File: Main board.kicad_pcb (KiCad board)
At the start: 4 copper layers, 50 x 75 mm, 106 parts, among them CN1 PA001-6P, CN2 PA001-6P, J1 Conn_ARM_SWD_TagConnect_TC203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, J2 Conn_01x02_Pin, J3 Conn_01x02_Pin, J5 Connector, USB-TYPE-C-16P, J6 436500201, J7 Conn_01x02_Pin, J8 Conn_01x04_Pin, Q1 SI7232DN-T1-GE3, Q2 SI7232DN-T1-GE3, SW1 SKRKAEE020, SW2 SKRKAEE020, SW3 SW_SPDT, SW4 SW_SPDT, U1 STM32U575VGTx, U10 TLV75733PDBV, U11 NRVB120VLSFT1G, U12 NRVB120VLSFT1G, U2 TPS62901RPJR, U3 MS5607-02BA03, U7 SN74AHCT125DR, U9 ICM-45686, X1 1XXD32000MBA, Y1 ECS-327TXO-33-TR

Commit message: Changed Pyro pour
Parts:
- moved J2 9.08 mm to (140.4, 102.1)
- moved SW3 2.01 mm to (133.4, 115.2)
- moved R5 1.40 mm to (139.7, 116.9)
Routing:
- net BEC+: track 14.2 -> 1.08 mm
- net PYRO+: track 5.84 -> 0.00 mm
- net Net-(SW3-B): track 4.69 -> 6.17 mm
- added copper zone on In2.Cu, net PYRO+
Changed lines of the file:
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@@
 	(footprint "PCM_JLCPCB:R_0402"
 		(layer "F.Cu")
-		(at 138.3067 116.7731)
+		(at 139.7 116.9)
 		(descr "Resistor SMD 0402 (1005 Metric), square (rectangular) end terminal, IPC_7351 nominal, (Body size source: IPC-SM-782 page 72, https://www.pcb-3d.com/wordpress/wp-content/uploads/ipc-sm-782a_amendment_1_and_2.pdf), generated with kicad-footprint-generator")
 		(tags "resistor")
@@
 	(footprint "Connector_PinHeader_2.54mm:PinHeader_1x02_P2.54mm_Vertical"
 		(layer "F.Cu")
-		(at 139.675 111.15 -90)
+		(at 140.375 102.1 -90)
 		(descr "Through hole straight pin header, 1x02, 2.54mm pitch, single row")
 		(tags "Through hole pin header THT 1x02 2.54mm single row")
@@
 	(footprint "EasyEDA:SW-TH_3P-L8.8-W3.9-P2.50_SS12D00G3"
 		(layer "F.Cu")
-		(at 131.4 115.4 180)
+		(at 133.4 115.2 180)
 		(property "Reference" "SW3"
 			(at 0 -4 0)
@@
 	)
 	(segment
-		(start 157.1675 120.8625)
-		(end 157.1675 123.3825)
-		(width 2)
-		(layer "F.Cu")
-		(net 10)
-	)
-	(segment
-		(start 124.251501 82.3736)
-		(end 123.827501 82.7976)
+		(start 133.4 115.2)
+		(end 133.4 117.3)
 		(width 2.5)
 		(layer "F.Cu")
-		(net 10)
+		(net 20)
 	)
 	(segment
-		(start 126.945001 82.3736)
-		(end 124.251501 82.3736)
+		(start 133.4 117.3)
+		(end 132.1675 118.5325)
 		(width 2.5)
 		(layer "F.Cu")
-		(net 10)
-	)
-	(segment
-		(start 157.1675 123.3825)
-		(end 157.15 123.4)
-		(width 2)
-		(layer "F.Cu")
-		(net 10)
+		(net 20)
 	)
 	(segment
-		(start 131.4 115.4)
-		(end 131.4 120.095)
-		(width 2)
+		(start 132.1675 118.5325)
+		(end 132.1675 120.8625)
+		(width 2.5)
 		(layer "F.Cu")
 		(net 20)
@@
 	)
 	(segment
-		(start 137.135 111.15)
-		(end 137.135 108.879869)
-		(width 2)
-		(layer "In2.Cu")
-		(net 36)
-	)
-	(segment
-		(start 137.135 111.15)
-		(end 137.135 112.165)
-		(width 2)
-		(layer "In2.Cu")
-		(net 36)
-	)
-	(segment
-		(start 137.135 112.165)
-		(end 133.9 115.4)
-		(width 2)
-		(layer "In2.Cu")
-		(net 36)
-	)
-	(segment
 		(start 133.405131 105.15)
 		(end 132.327501 105.15)
@@
 	)
 	(segment
-		(start 137.135 108.879869)
-		(end 133.405131 105.15)
-		(width 2)
-		(layer "In2.Cu")
-		(net 36)
-	)
-	(segment
 		(start 144.314401 92.096)
 		(end 144.244337 92.166064)
@@
 	)
 	(zone
-		(net 10)
-		(net_name "PYRO+")
+		(net 65)
+		(net_name "MS5607_CS")
 		(layer "F.Cu")
-		(name "PYRO+")
-		(hatch full 0.5)
+		(name "$teardrop_padvia$")
+		(hatch none 0.1)
+		(priority 30002)
+		(attr
+			(teardrop
+				(type padvia)
+			)
+		)
 		(connect_pads yes
 			(clearance 0)
 		)
-		(min_thickness 0.25)
+		(min_thickness 0.0254)
 		(filled_areas_thickness no)
 		(fill yes
 			(thermal_gap 0.5)
 			(thermal_bridge_width 0.5)
+			(island_removal_mode 1)
+			(island_area_min 10)
 		)
 		(polygon
 			(pts
-				(xy 160.65 123.15) (xy 161.65 123.65) (xy 161.65 126.4) (xy 121.9 126.4) (xy 121.4 125.9) (xy 121.4 123.15)
-				(xy 121.65 116.65) (xy 129.4 117.4) (xy 129.65 123.4)
+				(xy 144.04 72.509546) (xy 144.24 72.509546) (xy 144.49 72.159546) (xy 144.14 71.558546) (xy 143.79 72.159546)
 			)
 		)
@@
 	)
 	(zone
-		(net 65)
-		(net_name "MS5607_CS")
+		(net 135)
+		(net_name "HSE_IN")
 		(layer "F.Cu")
 		(name "$teardrop_padvia$")
 		(hatch none 0.1)
-		(priority 30001)
+		(priority 30006)
 		(attr
 			(teardrop
@@
 		(polygon
 			(pts
-				(xy 144.04 72.509546) (xy 144.24 72.509546) (xy 144.49 72.159546) (xy 144.14 71.558546) (xy 143.79 72.159546)
+				(xy 142.775382 85.696) (xy 142.775382 85.496) (xy 142.425382 85.469117) (xy 142.074382 85.919117)
+				(xy 142.425382 86.142719)
 			)
 		)
@@
 	)
 	(zone
-		(net 65)
-		(net_name "MS5607_CS")
+		(net 104)
+		(net_name "LSE_IN")
 		(layer "F.Cu")
 		(name "$teardrop_padvia$")
@@
 		(polygon
 			(pts
-				(xy 144.24 72.809546) (xy 144.04 72.809546) (xy 143.79 73.159546) (xy 144.14 73.760546) (xy 144.49 73.159546)
+				(xy 141.534391 83.696001) (xy 141.534391 83.496001) (xy 141.034391 82.991268) (xy 140.508391 83.3997)
+				(xy 141.034391 83.8997)
 			)
 		)
 	)
 	(zone
-		(net 10)
-		(net_name "PYRO+")
+		(net 1)
+		(net_name "VBAT-")
 		(layer "F.Cu")
-		(name "PYRO+")
-		(hatch full 0.5)
+		(name "$teardrop_padvia$")
+		(hatch none 0.1)
+		(priority 30004)
+		(attr
+			(teardrop
+				(type padvia)
+			)
+		)
 		(connect_pads yes
 			(clearance 0)
 		)
-		(min_thickness 0.25)
+		(min_thickness 0.0254)
 		(filled_areas_thickness no)
 		(fill yes
 			(thermal_gap 0.5)
 			(thermal_bridge_width 0.5)
+			(island_removal_mode 1)
+			(island_area_min 10)
 		)
 		(polygon
 			(pts
-				(xy 124.794282 108.224472) (xy 128.353932 110.735673) (xy 131.15 109.15) (xy 133.533755 109.15)
-				(xy 133.991865 109.774999) (xy 133.4 111.65) (xy 129.9 112.9) (xy 129.4 119.15) (xy 121.4 119.15)
-				(xy 121.527306 75.349634) (xy 122.600657 74.276283) (xy 126.480883 74.202008) (xy 127.414901 75.154949)
-				(xy 127.323018 77.497975) (xy 126.729101 78.095) (xy 124.456342 78.095)
+				(xy 145.95 71.459547) (xy 145.950001 71.659546) (xy 146.3 71.909546) (xy 146.650999 71.559546) (xy 146.3 71.209546)
 			)
 		)
@@
 	)
 	(zone
-		(net 135)
-		(net_name "HSE_IN")
-		(layer "F.Cu")
-		(name "$teardrop_padvia$")
-		(hatch none 0.1)
-		(priority 30001)
-		(attr
-			(teardrop
-				(type padvia)
-			)
-		)
-		(connect_pads yes
-			(clearance 0)
-		)
-		(min_thickness 0.0254)
-		(filled_areas_thickness no)
-		(fill yes
-			(thermal_gap 0.5)
-			(thermal_bridge_width 0.5)
-			(island_removal_mode 1)
-			(island_area_min 10)
-		)
-		(polygon
-			(pts
-				(xy 142.775382 85.696) (xy 142.775382 85.496) (xy 142.425382 85.469117) (xy 142.074382 85.919117)
-				(xy 142.425382 86.142719)
-			)
-		)
-	)
-	(zone
 		(net 10)
 		(net_name "PYRO+")
@@
 		(name "$teardrop_padvia$")
 		(hatch none 0.1)
-		(priority 30004)
+		(priority 30005)
 		(attr
 			(teardrop
@@
 	)
 	(zone
-		(net 104)
-		(net_name "LSE_IN")
-		(layer "F.Cu")
-		(name "$teardrop_padvia$")
-		(hatch none 0.1)
-		(priority 30000)
-		(attr
-			(teardrop
-				(type padvia)
-			)
-		)
-		(connect_pads yes
-			(clearance 0)
-		)
-		(min_thickness 0.0254)
-		(filled_areas_thickness no)
-		(fill yes
-			(thermal_gap 0.5)
-			(thermal_bridge_width 0.5)
-			(island_removal_mode 1)
-			(island_area_min 10)
-		)
-		(polygon
-			(pts
-				(xy 141.534391 83.696001) (xy 141.534391 83.496001) (xy 141.034391 82.991268) (xy 140.508391 83.3997)
-				(xy 141.034391 83.8997)
-			)
-		)
-	)
-	(zone
-		(net 28)
-		(net_name "Net-(D4-A)")
+		(net 141)
+		(net_name "Net-(CN2-Pad3)")
 		(layer "F.Cu")
-		(name "$teardrop_padvia$")
-		(hatch none 0.1)
-		(priority 30002)
-		(attr
-			(teardrop
-				(type padvia)
-			)
-		)
+		(name "CN2-Pad3")
+		(hatch full 0.5)
+		(priority 4)
 		(connect_pads yes
 			(clearance 0)
 		)
-		(min_thickness 0.0254)
+		(min_thickness 0.25)
 		(filled_areas_thickness no)
 		(fill yes
 			(thermal_gap 0.5)
 			(thermal_bridge_width 0.5)
-			(island_removal_mode 1)
-			(island_area_min 10)
 		)
 		(polygon
 			(pts
-				(xy 143.120002 69.159547) (xy 143.120002 69.359547) (xy 143.520002 69.659547) (xy 143.921002 69.259548)
-				(xy 143.520002 68.859548)
+				(xy 132.577501 84.5476) (xy 133.827501 84.5476) (xy 133.827501 88.7671) (xy 132.577501 88.7671)
 			)
 		)
 	)
 	(zone
-		(net 141)
-		(net_name "Net-(CN2-Pad3)")
+		(net 139)
+		(net_name "Net-(CN1-Pad5)")
 		(layer "F.Cu")
-		(name "CN2-Pad3")
+		(name "CN1-Pad3")
 		(hatch full 0.5)
 		(priority 4)
@@
 		(polygon
 			(pts
-				(xy 132.577501 84.5476) (xy 133.827501 84.5476) (xy 133.827501 88.7671) (xy 132.577501 88.7671)
+				(xy 156.3692 115.5793) (xy 156.3692 116.829301) (xy 152.1497 116.829301) (xy 152.1497 115.5793)
 			)
 		)
 	)
 	(zone
-		(net 139)
-		(net_name "Net-(CN1-Pad5)")
+		(net 28)
+		(net_name "Net-(D4-A)")
 		(layer "F.Cu")
-		(name "CN1-Pad3")
-		(hatch full 0.5)
-		(priority 4)
+		(name "$teardrop_padvia$")
+		(hatch none 0.1)
+		(priority 30003)
+		(attr
+			(teardrop
+				(type padvia)
+			)
+		)
 		(connect_pads yes
 			(clearance 0)
 		)
-		(min_thickness 0.25)
+		(min_thickness 0.0254)
 		(filled_areas_thickness no)
 		(fill yes
 			(thermal_gap 0.5)
 			(thermal_bridge_width 0.5)
+			(island_removal_mode 1)
+			(island_area_min 10)
 		)
 		(polygon
 			(pts
-				(xy 156.3692 115.5793) (xy 156.3692 116.829301) (xy 152.1497 116.829301) (xy 152.1497 115.5793)
+				(xy 143.120002 69.159547) (xy 143.120002 69.359547) (xy 143.520002 69.659547) (xy 143.921002 69.259548)
+				(xy 143.520002 68.859548)
 			)
 		)
@@
 	)
 	(zone
-		(net 1)
-		(net_name "VBAT-")
+		(net 65)
+		(net_name "MS5607_CS")
 		(layer "F.Cu")
 		(name "$teardrop_padvia$")
 		(hatch none 0.1)
-		(priority 30003)
+		(priority 30001)
 		(attr
 			(teardrop
@@
 		(polygon
 			(pts
-				(xy 145.95 71.459547) (xy 145.950001 71.659546) (xy 146.3 71.909546) (xy 146.650999 71.559546) (xy 146.3 71.209546)
+				(xy 144.24 72.809546) (xy 144.04 72.809546) (xy 143.79 73.159546) (xy 144.14 73.760546) (xy 144.49 73.159546)
+			)
+		)
+	)
+	(zone
+		(net 10)
+		(net_name "PYRO+")
+		(layer "In2.Cu")
+		(name "PYRO+")
+		(hatch full 0.5)
+		(priority 6)
+		(connect_pads yes
+			(clearance 0.6)
+		)
+		(min_thickness 0.25)
+		(filled_areas_thickness no)
+		(fill yes
+			(thermal_gap 0.5)
+			(thermal_bridge_width 0.5)
+		)
+		(polygon
+			(pts
+				(xy 121.65 73.65) (xy 129.8 73.65) (xy 130.7 74.55) (xy 130.410508 112.039213) (xy 132.783966 116.8493)
+				(xy 159.6 118.3) (xy 159.7 118.4) (xy 159.7 126.2) (xy 159.5 126.4) (xy 128.3 126.4) (xy 128.1 126.2)
+				(xy 128.1 120.8625) (xy 126.7375 119.5) (xy 122.4 119.5) (xy 121.3 118.4) (xy 121.3 73.9)
 			)
 		)

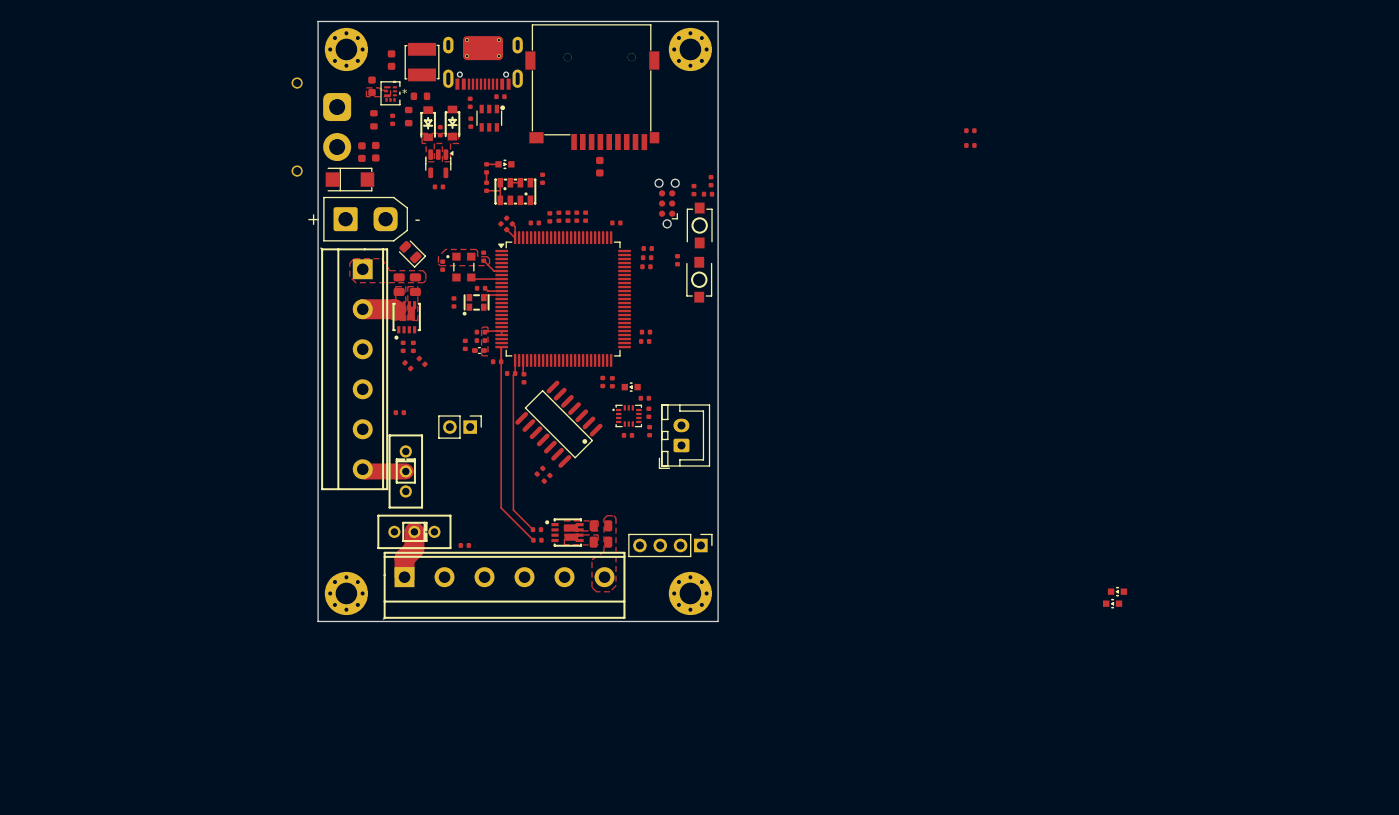
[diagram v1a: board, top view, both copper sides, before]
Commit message: Change switch footprint to C&K 1101M2S3CQE2
For handling PYRO power and temp
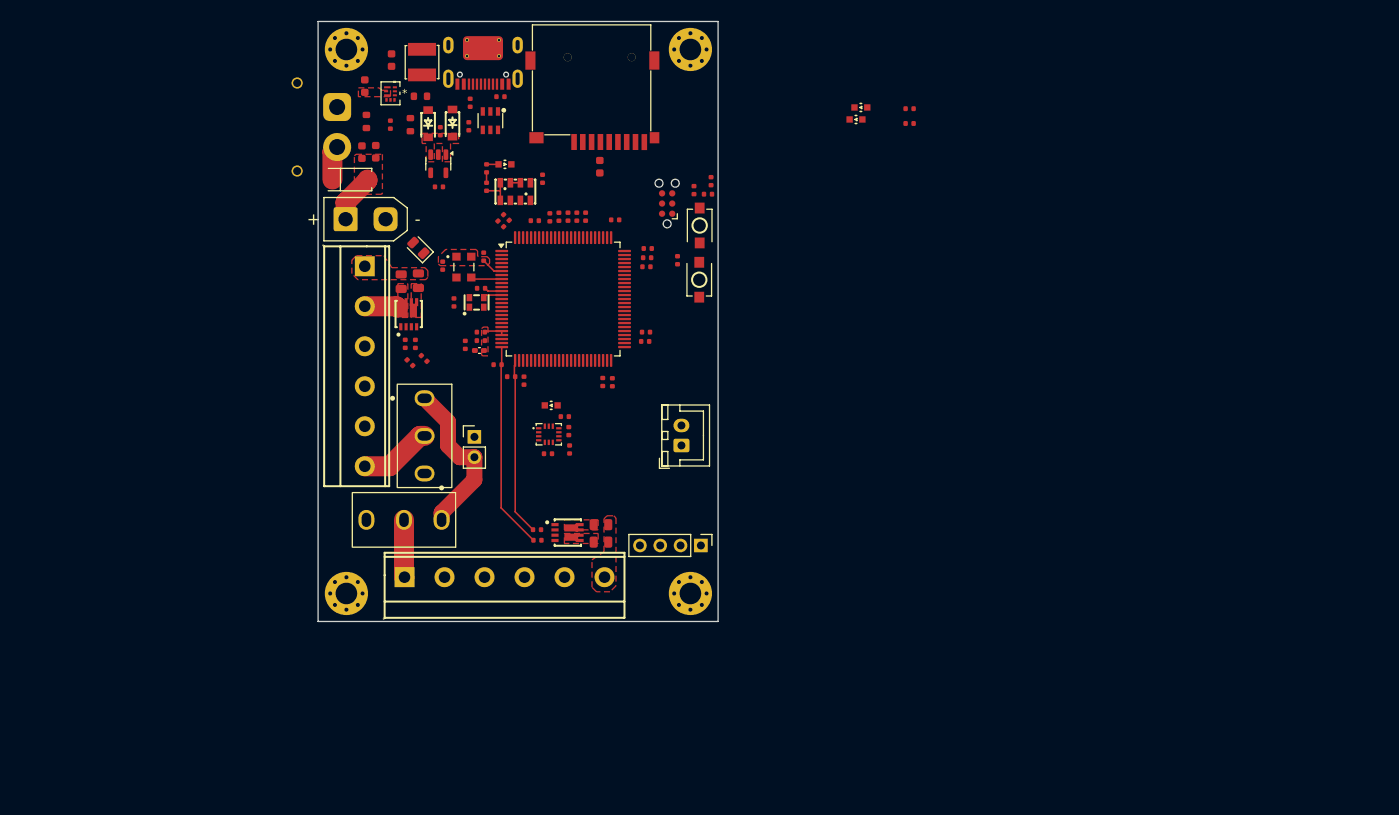
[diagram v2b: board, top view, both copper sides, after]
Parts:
- removed C15: 100nF, PCM_JLCPCB:C_0402
- removed C25: 10uF, PCM_JLCPCB:C_0402
- removed R5, R8: 75Ω, PCM_JLCPCB:R_0402
- removed U7: SN74AHCT125DR, EASYEDA:SOIC-14_L8.7-W3.9-P1.27-LS6.0-BL
- J6: value 436500201 -> XT30UPB-F
- SW3, SW4: footprint EasyEDA:SW-TH_3P-L8.8-W3.9-P2.50_SS12D00G3 -> Mainboard_local:SW-TH_1101M2S3CQE2
- moved D6 68.5 mm to (188.6, 63.6)
- moved D5 68.5 mm to (189.2, 62.1)
- moved C17 10.3 mm to (150.1, 105.4)
- moved C19 10.3 mm to (152.8, 104.9)
- moved D7 10.3 mm to (150.5, 99.4)
- moved R18 10.3 mm to (152.2, 100.8)
- moved U9 10.3 mm to (150.2, 103.0)
- moved R31 10.3 mm to (152.7, 102.6)
- moved R14 8.08 mm to (195.3, 64.2)
- moved R6 8.08 mm to (195.3, 62.3)
- moved SW4 5.03 mm to (134.7, 103.2)
- moved SW3 1.98 mm to (132.1, 113.7)
- moved J2 1.33 mm to (140.9, 103.3), turned to 0 degrees
- moved JP1 1.12 mm to (133.9, 79.7)
- moved R24 1.04 mm to (132.9, 64.3)
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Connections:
- U1 pad 40: PWM1 -> SERVO1
- U1 pad 42: PWM2 -> SERVO2
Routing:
- net BEC+: track 1.08 -> 20.6 mm
- net PYRO+: track 0.00 -> 6.09 mm
- net +3V3: track 11.4 -> 6.36 mm
- net VBAT+: track 0.00 -> 4.31 mm
- net Net-(SW4-B): track 5.50 -> 9.04 mm
- net FIRE_A: track 22.3 -> 20.0 mm
- net Net-(SW3-B): track 6.17 -> 7.19 mm

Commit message: New layout New.ioc
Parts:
- CN1, CN2: value PA001-6P -> KF127S-3.5-6P; footprint Mainboard_local:CONN-TH_6P-P5.00_PA001-6P -> TerminalBlock_Phoenix:TerminalBlock_Phoenix_PT-1,5-6-3.5-H_1x06_P3.50mm_Horizontal
- H1, H2, H3, H4: footprint MountingHole:MountingHole_2.7mm_M2.5_Pad_Via -> MountingHole:MountingHole_2.2mm_M2_Pad_Via
- J3: value Conn_01x02_Pin -> Micro-Fit 43650-0215; footprint Connector_AMASS:AMASS_XT30PW-F_1x02_P2.50mm_Horizontal -> Connector_Molex:Molex_Micro-Fit_3.0_43650-0215_1x02_P3.00mm_Vertical; moved to F.Cu
- J6: value XT30UPB-F -> Micro-Fit 43650-0215; footprint Connector_AMASS:AMASS_XT30UPB-F_1x02_P5.0mm_Vertical -> Connector_Molex:Molex_Micro-Fit_3.0_43650-0215_1x02_P3.00mm_Vertical
- JP3: renamed from SW3; value SW_SPDT -> BEC 1-2 / PYRO 2-3; footprint Mainboard_local:SW-TH_1101M2S3CQE2 -> Jumper:SolderJumper-3_P1.3mm_Open_Pad1.0x1.5mm_NumberLabels
- JP4: renamed from SW4; value SW_SPDT -> BEC 1-2 / PYRO 2-3; footprint Mainboard_local:SW-TH_1101M2S3CQE2 -> Jumper:SolderJumper-3_P1.3mm_Open_Pad1.0x1.5mm_NumberLabels
- moved C17 104.0 mm to (245.3, 63.6)
- moved R18 104.0 mm to (247.4, 59.0)
- moved U9 104.0 mm to (245.4, 61.2)
- moved R31 104.0 mm to (247.9, 60.8)
- moved C19 104.0 mm to (248.0, 63.1)
- moved D7 104.0 mm to (245.7, 57.5)
- moved C28 96.1 mm to (205.4, 116.5), turned to 0 degrees
- moved L1 95.3 mm to (205.2, 120.3), turned to 180 degrees
- moved J5 95.0 mm to (204.9, 127.9), turned to 90 degrees
- moved C27 92.2 mm to (202.2, 113.1), turned to 0 degrees
- moved U2 90.3 mm to (201.3, 116.3), turned to -90 degrees
- moved R22 89.5 mm to (200.8, 130.1), turned to -90 degrees
- moved R26 89.3 mm to (200.9, 120.1), turned to 90 degrees
- moved R23 88.1 mm to (200.1, 126.3), turned to 180 degrees
- moved R25 86.0 mm to (197.7, 113.3), turned to 180 degrees
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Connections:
- CN1 pad 1: Net-(SW3-B) -> Net-(CN1-Pad1)
- CN1 pad 2: SERVO1 -> Net-(CN1-Pad2)
- CN1 pad 4: Net-(CN1-Pad4) -> SERVO1
- CN1 pad 5: Net-(CN1-Pad5) -> Net-(JP3-C)
- CN2 pad 2: Net-(CN2-Pad2) -> Net-(JP4-C)
- CN2 pad 3: Net-(CN2-Pad3) -> SERVO2
- CN2 pad 5: SERVO2 -> Net-(CN2-Pad5)
- CN2 pad 6: Net-(SW4-B) -> Net-(CN2-Pad6)
- JP3 pad 2: Net-(SW3-B) -> Net-(JP3-C)
- JP4 pad 2: Net-(SW4-B) -> Net-(JP4-C)
- Q1 pad 5: Net-(CN1-Pad5) -> Net-(CN1-Pad1)
- Q1 pad 6: Net-(CN1-Pad5) -> Net-(CN1-Pad1)
- Q1 pad 7: Net-(CN1-Pad4) -> Net-(CN1-Pad2)
- Q1 pad 8: Net-(CN1-Pad4) -> Net-(CN1-Pad2)
- Q2 pad 5: Net-(CN2-Pad3) -> Net-(CN2-Pad5)
- Q2 pad 6: Net-(CN2-Pad3) -> Net-(CN2-Pad5)
- Q2 pad 7: Net-(CN2-Pad2) -> Net-(CN2-Pad6)
- Q2 pad 8: Net-(CN2-Pad2) -> Net-(CN2-Pad6)
- R2 pad 1: FIRE_B -> FIRE_A
- R32 pad 1: FIRE_A -> FIRE_B
- R35 pad 1: FIRE_A -> FIRE_B
- R36 pad 1: FIRE_B -> FIRE_A
- R40 pad 2: Net-(CN1-Pad4) -> Net-(CN1-Pad2)
- R41 pad 2: Net-(CN1-Pad5) -> Net-(CN1-Pad1)
- R42 pad 2: Net-(CN2-Pad3) -> Net-(CN2-Pad5)
- R43 pad 2: Net-(CN2-Pad2) -> Net-(CN2-Pad6)
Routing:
- net FIRE_B: track 25.9 -> 0.00 mm
- net BEC+: track 20.6 -> 0.00 mm
- net FIRE_A: track 20.0 -> 0.00 mm
- net Net-(SW4-B): track 9.04 -> 0.00 mm
- net Net-(SW3-B): track 7.19 -> 0.00 mm
- net PYRO+: track 6.09 -> 0.00 mm
- net Net-(CN2-Pad2): track 4.20 -> 0.00 mm
- net VBAT+: track 4.31 -> 6.13 mm
- added copper zone on F.Cu, net Net-(CN1-Pad1)
- added copper zone on F.Cu, net Net-(CN1-Pad2)
- added copper zone on F.Cu, net Net-(CN2-Pad5)
- removed copper zone on F.Cu, net Net-(CN1-Pad4)
- removed copper zone on F.Cu, net Net-(CN1-Pad5)
- removed copper zone on F.Cu, net Net-(CN2-Pad2)
- removed copper zone on F.Cu, net Net-(CN2-Pad3)
- removed copper zone on In2.Cu, net PYRO+
